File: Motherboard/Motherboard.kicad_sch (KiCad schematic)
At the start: 53 parts, among them J1 40-pin IDE Connector, J3 Bus_ISA_8bit, J4 ATX-24, J5 USB_B, J6 ATF15XX_JTAG_ISP, J7 Bus_ISA_8bit, J8 65SIB_Connector, SW1 SW_Push, SW2 SW_SPST, U1 AS6C8008, U10 ATF1508AS-PLCC84, U11 74HCT245, U12 74HCT573, U13 8255, U14 WD65C22, U15 AS6C8008, U16 MCP2200-I-SO, U17 74HCT163, U18 LM7905_TO220, U19 GAL16V8, U2 74HCT04, U3 SC28L91, U4 SST39SF040, U5 SST39SF040, U6 SST39SF040, U7 SST39SF040, U8 WD65C816S, U9 DS1813, X1 ACO-3.6864MHz, X2 ACO-24MHz, X3 ACO-14.31818MHz

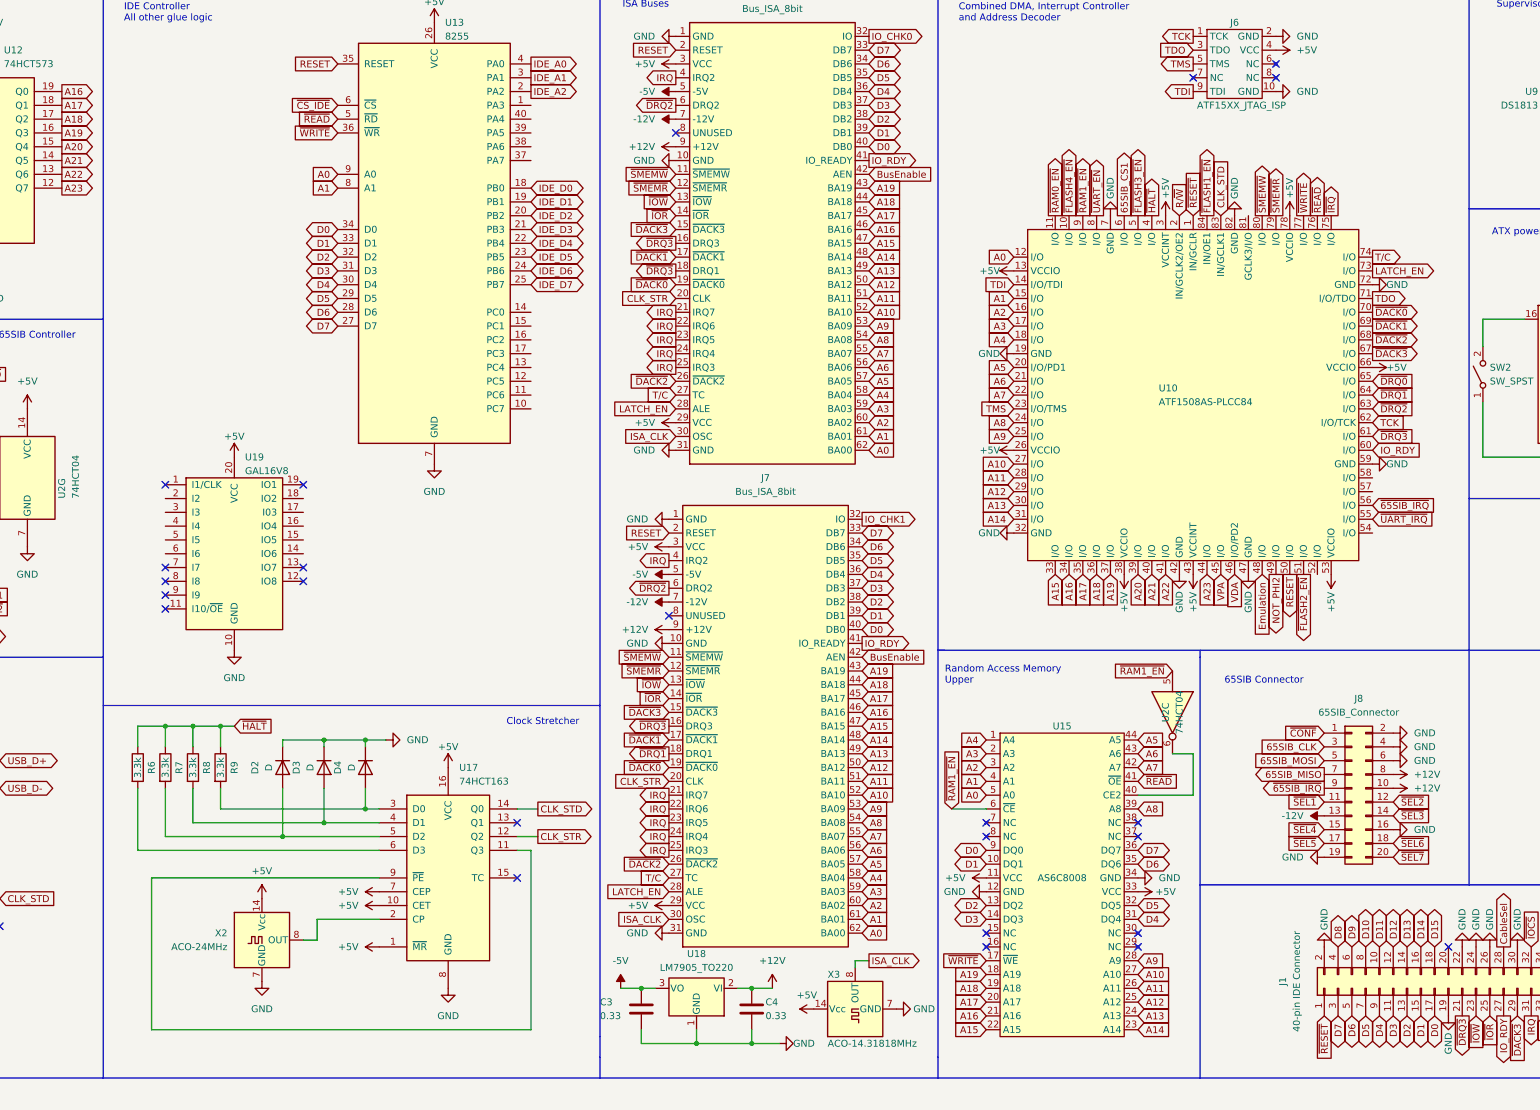
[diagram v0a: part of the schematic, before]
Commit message: Update Motherboard.kicad_sch
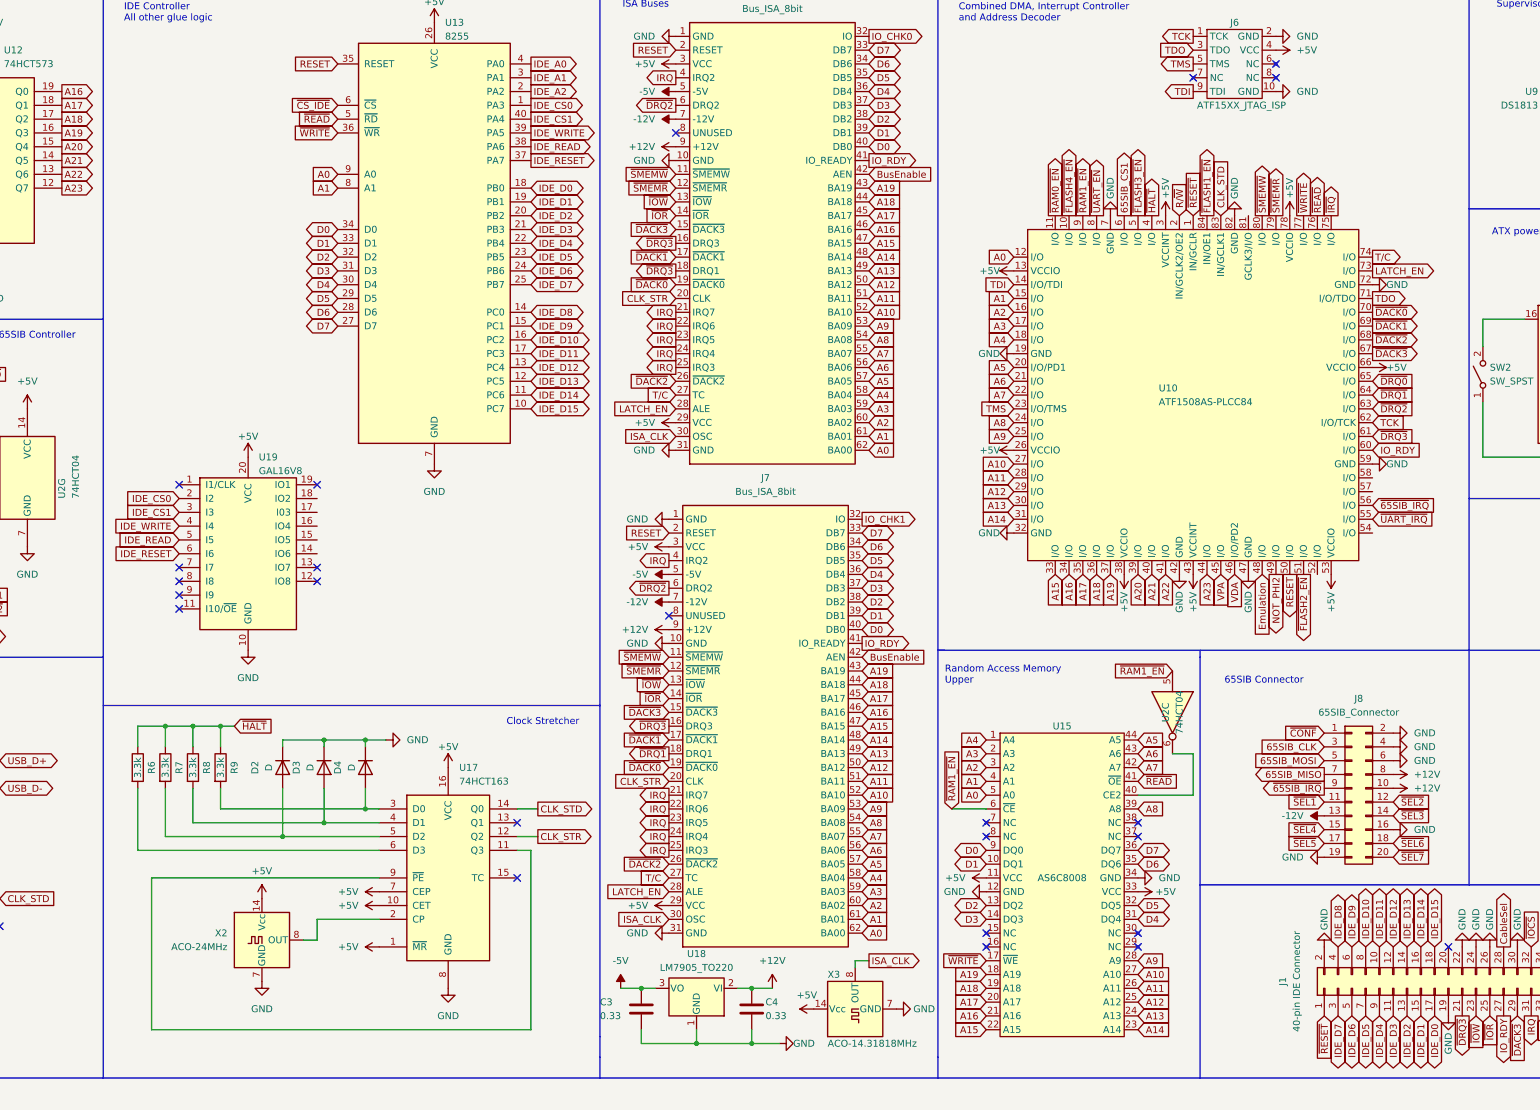
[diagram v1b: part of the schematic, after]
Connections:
- net D10 is gone; now on net IDE_D10: J1.8 (Pin_8)
- net D11 is gone; now on net IDE_D11: J1.10 (Pin_10)
- net D12 is gone; now on net IDE_D12: J1.12 (Pin_12)
- net D13 is gone; now on net IDE_D13: J1.14 (Pin_14)
- net D14 is gone; now on net IDE_D14: J1.16 (Pin_16)
- net D15 is gone; now on net IDE_D15: J1.18 (Pin_18)
- net D9 is gone; now on net IDE_D9: J1.6 (Pin_6)
- net D0: no longer J1.17 (Pin_17)
- net D1: no longer J1.15 (Pin_15)
- net D2: no longer J1.13 (Pin_13)
- net D3: no longer J1.11 (Pin_11)
- net D4: no longer J1.9 (Pin_9)
- net D5: no longer J1.7 (Pin_7)
- net D6: no longer J1.5 (Pin_5)
- net D7: no longer J1.3 (Pin_3)
- net D8: no longer J1.4 (Pin_4)
- net IDE_D0: now also J1.17 (Pin_17)
- net IDE_D1: now also J1.15 (Pin_15)
- net IDE_D2: now also J1.13 (Pin_13)
- net IDE_D3: now also J1.11 (Pin_11)
- net IDE_D4: now also J1.9 (Pin_9)
- net IDE_D5: now also J1.7 (Pin_7)
- net IDE_D6: now also J1.5 (Pin_5)
- net IDE_D7: now also J1.3 (Pin_3)
- net IDE_CS0: now reaches U13.1 (PA3)
- net IDE_CS0: now also U19.2 (I2)
- net IDE_D15: now reaches U13.10 (PC7)
- net IDE_D14: now reaches U13.11 (PC6)
- net IDE_D13: now reaches U13.12 (PC5)
- net IDE_D12: now reaches U13.13 (PC4)
- net IDE_D8: now reaches U13.14 (PC0)
- net IDE_D8: now also J1.4 (Pin_4)
- net IDE_D9: now reaches U13.15 (PC1)
- net IDE_D10: now reaches U13.16 (PC2)
- net IDE_D11: now reaches U13.17 (PC3)
- net IDE_RESET: now reaches U13.37 (PA7)
- net IDE_RESET: now also U19.6 (I6)
- net IDE_READ: now reaches U13.38 (PA6)
- net IDE_READ: now also U19.5 (I5)
- net IDE_WRITE: now reaches U13.39 (PA5)
- net IDE_WRITE: now also U19.4 (I4)
- net IDE_CS1: now reaches U13.40 (PA4)
- net IDE_CS1: now also U19.3 (I3)
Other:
- moved on the sheet: U19

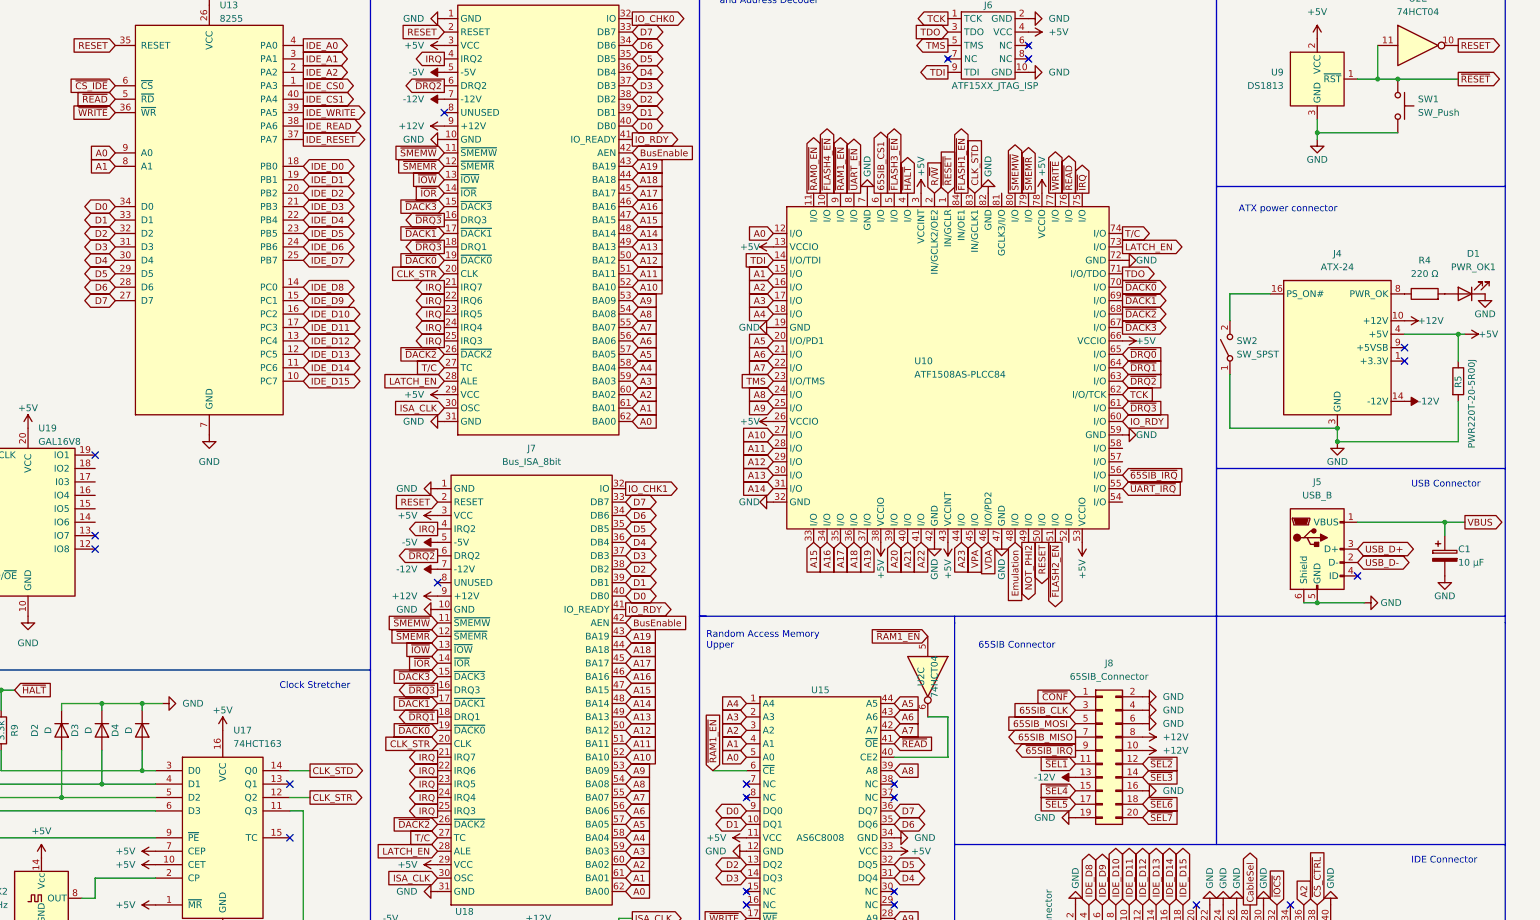
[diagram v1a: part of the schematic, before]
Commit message: Update IDE Interface, controller and added parts to PCB...
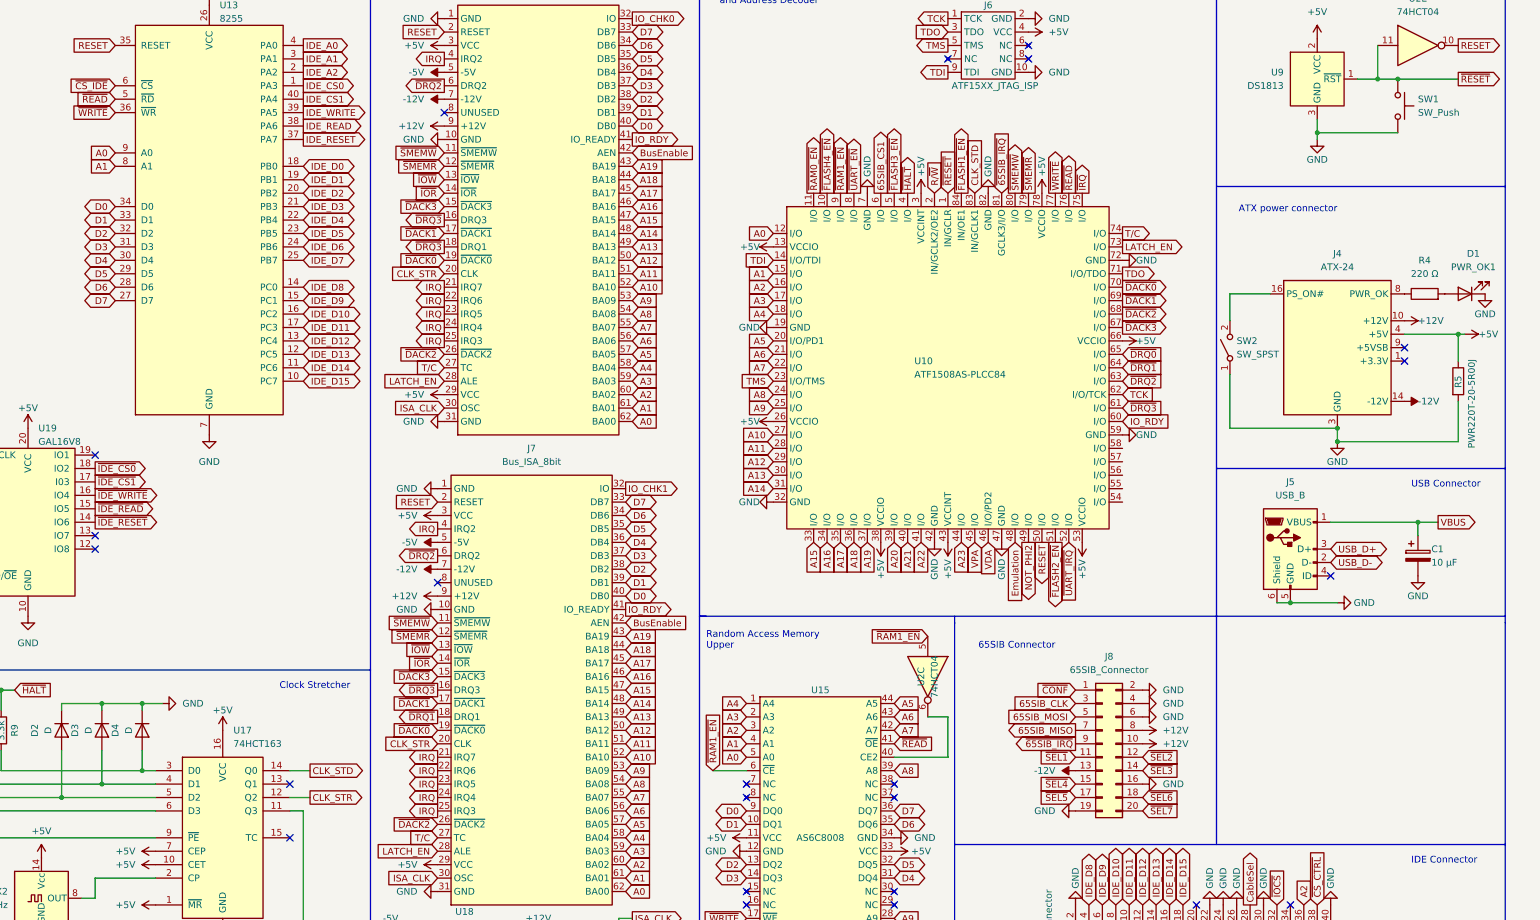
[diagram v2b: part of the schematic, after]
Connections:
- net ~{65SIB_IRQ}: now also U10.81 (GCLK3/I/O); no longer U10.56 (I/O)
- net ~{UART_IRQ}: now also U10.52 (I/O); no longer U10.55 (I/O)
- net ~{IDE_RESET}: now reaches U19.14 (IO6)
- net ~{IDE_READ}: now reaches U19.15 (IO5)
- net ~{IDE_WRITE}: now reaches U19.16 (IO4)
- net ~{IDE_CS1}: now reaches U19.17 (I03)
- net ~{IDE_CS0}: now reaches U19.18 (IO2)
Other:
- moved on the sheet: C1, J5, J8

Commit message: Fixed clock connections...
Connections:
- net CLK_STD: no longer U10.83 (IN/GCLK1), U8.37 (PHI2)
- net CLK_STR: now also U10.83 (IN/GCLK1), U8.37 (PHI2)
- net NOT_PHI2 renamed NOT_CLK_STR
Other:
- moved on the sheet: U10

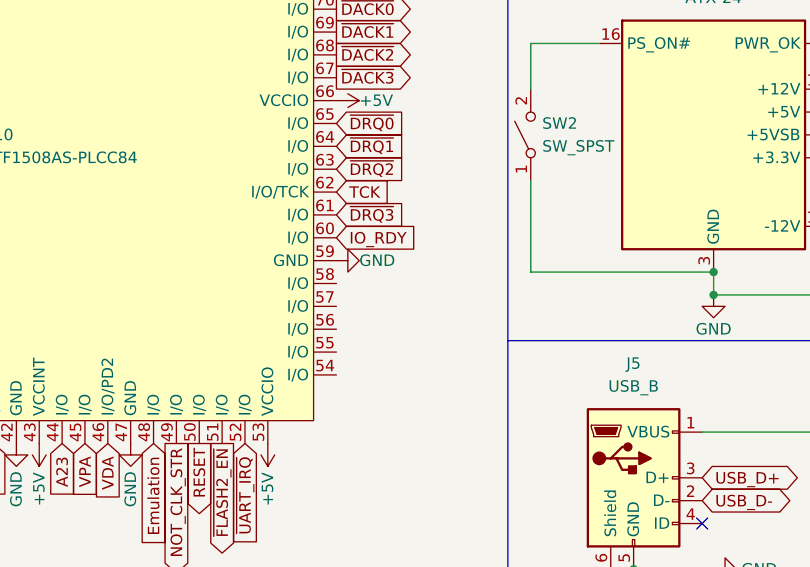
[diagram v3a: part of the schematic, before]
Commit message: 334 unrouted traces...
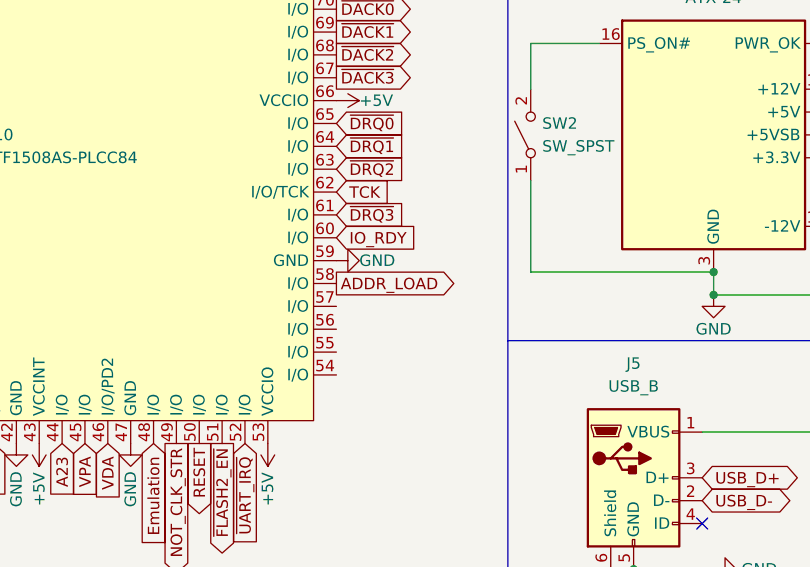
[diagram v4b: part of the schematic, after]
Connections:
- net ADDR_LOAD: now also U10.58 (I/O)
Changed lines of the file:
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@@
+    )
+  )
+  (global_label "ADDR_LOAD" (shape output) (at 436.88 233.68 0) (fields_autoplaced)
+    (effects (font (size 1.27 1.27)) (justify left))
+    (property "Intersheetrefs" "${INTERSHEET_REFS}" (at 450.3692 233.68 0)
+      (effects (font (size 1.27 1.27)) (justify left) hide)
     )
   )

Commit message: Replaced discontinued DUART and fixed wiring...
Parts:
- removed U3: SC28L91, Package_LCC:PLCC-44, symbol UART:SC28L91
- added D7: LED, symbol Device:LED
- added R12: 330, symbol Device:R
- added R13: 3.3k, Resistor_THT:R_Axial_DIN0207_L6.3mm_D2.5mm_P7.62mm_Horizontal, symbol Device:R
- added R14: 3.3k, symbol Device:R
- added U3: ~, symbol UART:XR88C92
- X1: value ACO-3.6864MHz -> ACO-xxxMHz
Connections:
- net ABORT is gone; now on net ~{ABORT}: U8.3 (ABORT)
- net CableSel is gone; now on net GND: J1.28 (Pin_28)
- net ~{CS_CMD} is gone; now on net ~{IDE_CS0}: J1.37 (Pin_37)
- net ~{CS_CTRL} is gone; now on net ~{IDE_CS1}: J1.38 (Pin_38)
- net ~{CS_IDE} is gone; now on net ~{IDE_EN}: U13.6 (~{CS})
- net +5V: now also R13.2, R14.2, U3.44 (VCC)
- net A0: now also U3.2 (A0); no longer J1.35 (Pin_35)
- net A1: now also U3.4 (A1); no longer J1.33 (Pin_33)
- net A2: now also U3.6 (A2); no longer J1.36 (Pin_36)
- net A3: now also U3.7 (A3)
- net D0: now also U3.28 (D0)
- net D1: now also U3.18 (D1)
- net D2: now also U3.27 (D2)
- net D3: now also U3.19 (D3)
- net D4: now also U3.26 (D4)
- net D5: now also U3.20 (D5)
- net D6: now also U3.25 (D6)
- net D7: now also U3.21 (D7)
- net GND: now also D7.1 (K), U3.22 (GND)
- net IDE_A0: now also J1.35 (Pin_35)
- net IDE_A1: now also J1.33 (Pin_33)
- net IDE_A2: now also J1.36 (Pin_36)
- net Memory/IndexSelect: now also U10.55 (I/O)
- net RESET: now also U3.38 (RESET)
- net RxD: now also U3.35 (RxA)
- net TxD: now also U3.33 (TxA)
- net ~{IDE_READ}: now also J1.25 (Pin_25)
- net ~{IDE_WRITE}: now also J1.23 (Pin_23)
- net ~{IOR}: no longer J1.25 (Pin_25)
- net ~{IOW}: no longer J1.23 (Pin_23)
- net ~{READ}: now also U3.10 (~{IOR})
- net ~{UART_EN}: now also U3.39 (~{CS})
- net ~{VectorPull}: now also U10.54 (I/O)
- net ~{WRITE}: now also U3.9 (~{IOW})
- net ~{ABORT}: now reaches U10.56 (I/O)
- net ~{IDE_EN}: now reaches U10.57 (I/O)
- net at JP1.2 (C): now also U3.24 (~{INT})
- net at X1.8 (OUT): now also U3.36 (XTAL1)
- net 65SIB_CS1: no longer names the net of U14.24 (CS1)
- net 65SIB_CS1: now also R13.1; no longer U10.6 (I/O)
- net ~{65SIB_CS2} renamed ~{65SIB_EN}
- net ~{65SIB_EN}: now also U10.6 (I/O)
- net ~{ACT}: no longer names the net of J1.39 (Pin_39)
- net ~{ACT}: now also R12.1
- net ~{IOCS}: no longer names the net of J1.32 (Pin_32)
- net ~{MemoryLock}: no longer names the net of U8.5 (~{ML})
- net ~{MemoryLock}: now also R14.1
- new net: D7.2 (A), R12.2
- no-connect marks 72 -> 71
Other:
- moved on the sheet: JP1, U2G

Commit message: Updated component footprints...
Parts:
- D7: footprint (none) -> LED_THT:LED_D5.0mm
- R12: footprint (none) -> Resistor_THT:R_Axial_DIN0207_L6.3mm_D2.5mm_P7.62mm_Horizontal
- U3: footprint (none) -> Package_LCC:PLCC-44_THT-Socket
- X1: value ACO-xxxMHz -> ACO-3.6864MHz
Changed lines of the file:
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@@
     (stroke (width 0) (type default))
   )
-  (wire (pts (xy 199.39 254) (xy 199.39 257.81))
+  (wire (pts (xy 201.93 254) (xy 201.93 257.81))
     (stroke (width 0) (type default))
   )
@@
     (stroke (width 0) (type default))
   )
-  (wire (pts (xy 194.31 257.81) (xy 199.39 257.81))
-    (stroke (width 0) (type default))
-  )
   (polyline (pts (xy 115.57 269.24) (xy 115.57 144.78))
     (stroke (width 0) (type default))
@@
     (stroke (width 0) (type default))
   )
+  (wire (pts (xy 194.31 257.81) (xy 201.93 257.81))
+    (stroke (width 0) (type default))
+  )
   (polyline (pts (xy 295.91 339.09) (xy 295.91 342.9))
     (stroke (width 0) (type default))
@@
       (effects (font (size 1.27 1.27)))
     )
-    (property "Footprint" "" (at 486.41 337.058 90)
+    (property "Footprint" "Resistor_THT:R_Axial_DIN0207_L6.3mm_D2.5mm_P7.62mm_Horizontal" (at 486.41 337.058 90)
       (effects (font (size 1.27 1.27)) hide)
     )
@@
       (effects (font (size 1.27 1.27)) (justify right))
     )
-    (property "Value" "ACO-xxxMHz" (at 497.84 99.695 0)
+    (property "Value" "ACO-3.6864MHz" (at 497.84 99.695 0)
       (effects (font (size 1.27 1.27)) (justify right))
     )
@@
       (effects (font (size 1.27 1.27)))
     )
-    (property "Footprint" "" (at 462.28 76.2 0)
+    (property "Footprint" "Package_LCC:PLCC-44_THT-Socket" (at 462.28 76.2 0)
       (effects (font (size 1.27 1.27)) hide)
     )
@@
     )
   )
-  (symbol (lib_name "+5V_5") (lib_id "power:+5V") (at 199.39 254 0) (unit 1)
+  (symbol (lib_name "+5V_5") (lib_id "power:+5V") (at 201.93 254 0) (unit 1)
     (in_bom yes) (on_board yes) (dnp no) (fields_autoplaced)
-    (property "Reference" "#PWR052" (at 199.39 257.81 0)
+    (property "Reference" "#PWR052" (at 201.93 257.81 0)
       (effects (font (size 1.27 1.27)) hide)
     )
-    (property "Value" "+5V" (at 199.39 250.19 0)
+    (property "Value" "+5V" (at 201.93 250.19 0)
       (effects (font (size 1.27 1.27)))
     )
-    (property "Footprint" "" (at 199.39 254 0)
+    (property "Footprint" "" (at 201.93 254 0)
       (effects (font (size 1.27 1.27)) hide)
     )
-    (property "Datasheet" "" (at 199.39 254 0)
+    (property "Datasheet" "" (at 201.93 254 0)
       (effects (font (size 1.27 1.27)) hide)
     )
@@
       (effects (font (size 1.27 1.27)))
     )
-    (property "Footprint" "" (at 494.03 335.28 0)
+    (property "Footprint" "LED_THT:LED_D5.0mm" (at 494.03 335.28 0)
       (effects (font (size 1.27 1.27)) hide)
     )
